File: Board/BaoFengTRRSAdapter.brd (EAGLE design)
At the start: 27.4 x 8.1 mm, 7 parts

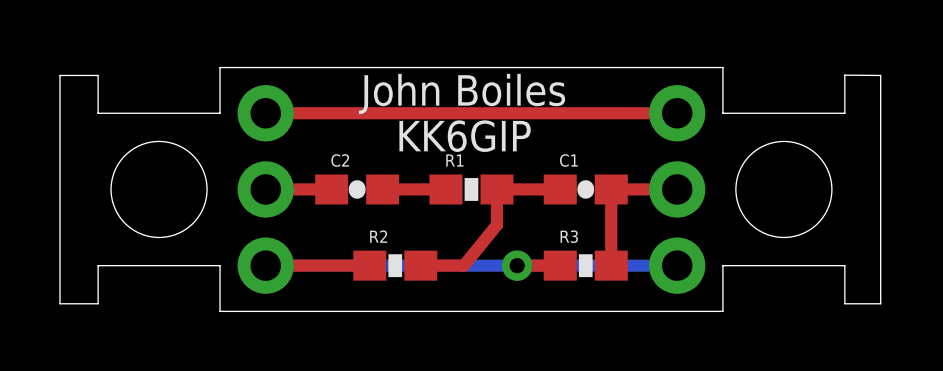
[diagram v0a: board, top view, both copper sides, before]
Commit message: Adding a ground plane as per suggestion by Chris Hood (KE5SBP)
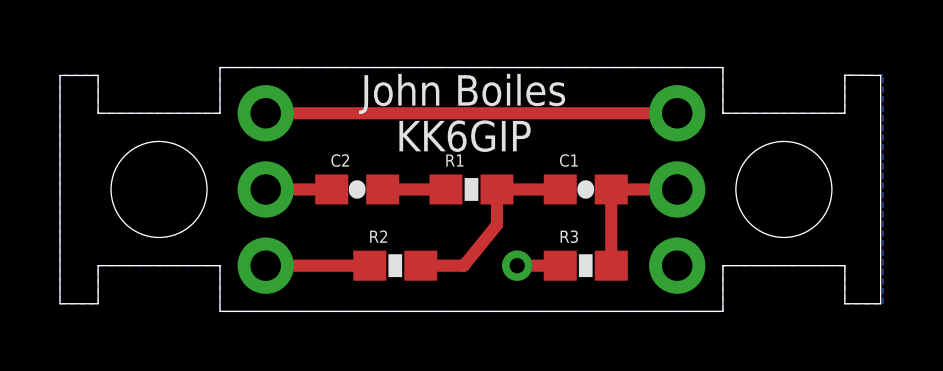
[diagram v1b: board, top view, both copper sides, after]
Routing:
- net GND: track 18.6 -> 4.90 mm
- added copper zone on layer 16, net GND
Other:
- board text added: "r3"
- board text removed: "r2"
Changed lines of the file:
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@@
 <text x="17.526" y="7.62" size="1.016" layer="25" align="center">John Boiles
 KK6GIP</text>
-<text x="18.034" y="3.048" size="0.8128" layer="26" rot="MR0" align="center">r2</text>
+<text x="18.034" y="3.048" size="0.8128" layer="26" rot="MR0" align="center">r3</text>
 <text x="22.86" y="2.54" size="0.8128" layer="26" rot="MR0" align="center">-</text>
 <text x="21.082" y="5.08" size="1.6764" layer="26" rot="MR270" align="center">TRRS</text>
@@
 <wire x1="20.74" y1="2.54" x2="19.304" y2="2.54" width="0.4064" layer="1"/>
 <contactref element="JP3" pad="1"/>
-<wire x1="24.638" y1="2.54" x2="19.304" y2="2.54" width="0.4064" layer="16"/>
 <contactref element="JP1" pad="1"/>
-<wire x1="10.922" y1="2.54" x2="19.304" y2="2.54" width="0.4064" layer="16"/>
 <wire x1="14.39" y1="2.54" x2="10.922" y2="2.54" width="0.4064" layer="1"/>
+<polygon width="0.4064" layer="16">
+<vertex x="4.064" y="8.89"/>
+<vertex x="4.064" y="1.27"/>
+<vertex x="5.334" y="1.27"/>
+<vertex x="5.334" y="2.54"/>
+<vertex x="9.398" y="2.54"/>
+<vertex x="9.398" y="1.016"/>
+<vertex x="26.162" y="1.016"/>
+<vertex x="26.162" y="2.54"/>
+<vertex x="30.226" y="2.54"/>
+<vertex x="30.226" y="1.27"/>
+<vertex x="31.496" y="1.27"/>
+<vertex x="31.496" y="8.89"/>
+<vertex x="30.226" y="8.89"/>
+<vertex x="30.226" y="7.62"/>
+<vertex x="26.162" y="7.62"/>
+<vertex x="26.162" y="9.144"/>
+<vertex x="9.398" y="9.144"/>
+<vertex x="9.398" y="7.62"/>
+<vertex x="5.334" y="7.62"/>
+<vertex x="5.334" y="8.89"/>
+</polygon>
 </signal>
 <signal name="N$3">
@@
 </signal>
 </signals>
+<errors>
+</errors>
 </board>
 </drawing>

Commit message: update to improve detection on various phones (#19)
Co-authored-by: kronicd <aaa>
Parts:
- added R4: 0.1k, SparkFun-Passives:0603-RES
- moved R1 0.76 mm to (17.8, 4.32)
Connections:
- net BAOFENGMIC+: now also R4.2
- net GND: now also R4.1
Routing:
- net GND: track 4.90 -> 6.29 mm, vias 1 -> 2
- net BAOFENGMIC+: track 13.7 -> 15.0 mm
